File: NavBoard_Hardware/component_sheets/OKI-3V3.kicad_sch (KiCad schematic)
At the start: 4 parts, among them U4 OKI-3V3

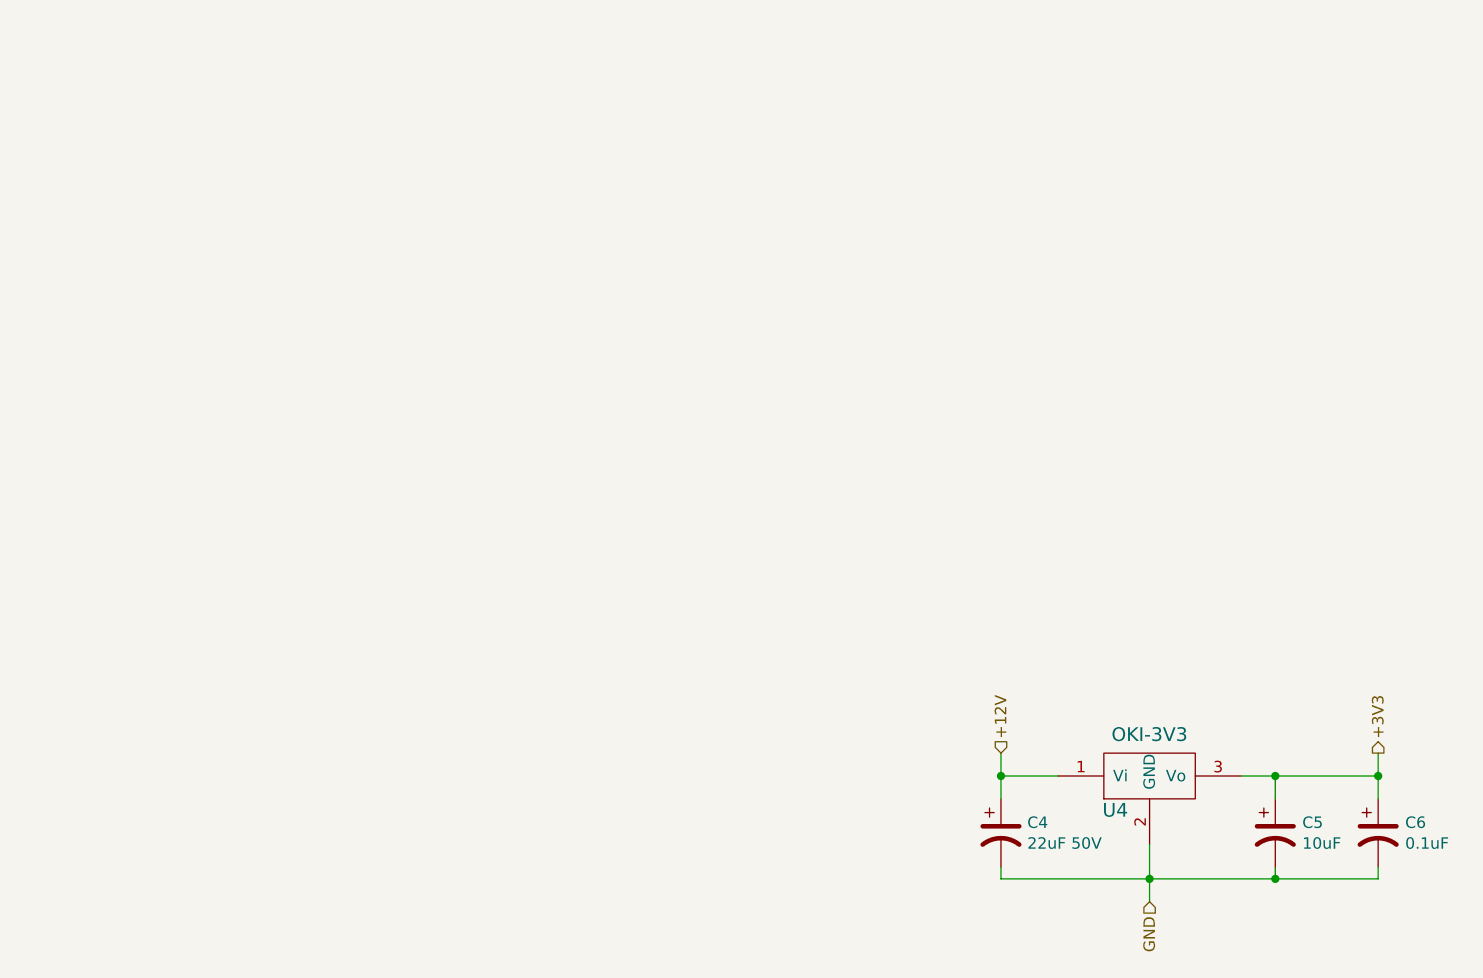
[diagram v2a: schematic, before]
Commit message: Corrected accelerometer regulator capacitors
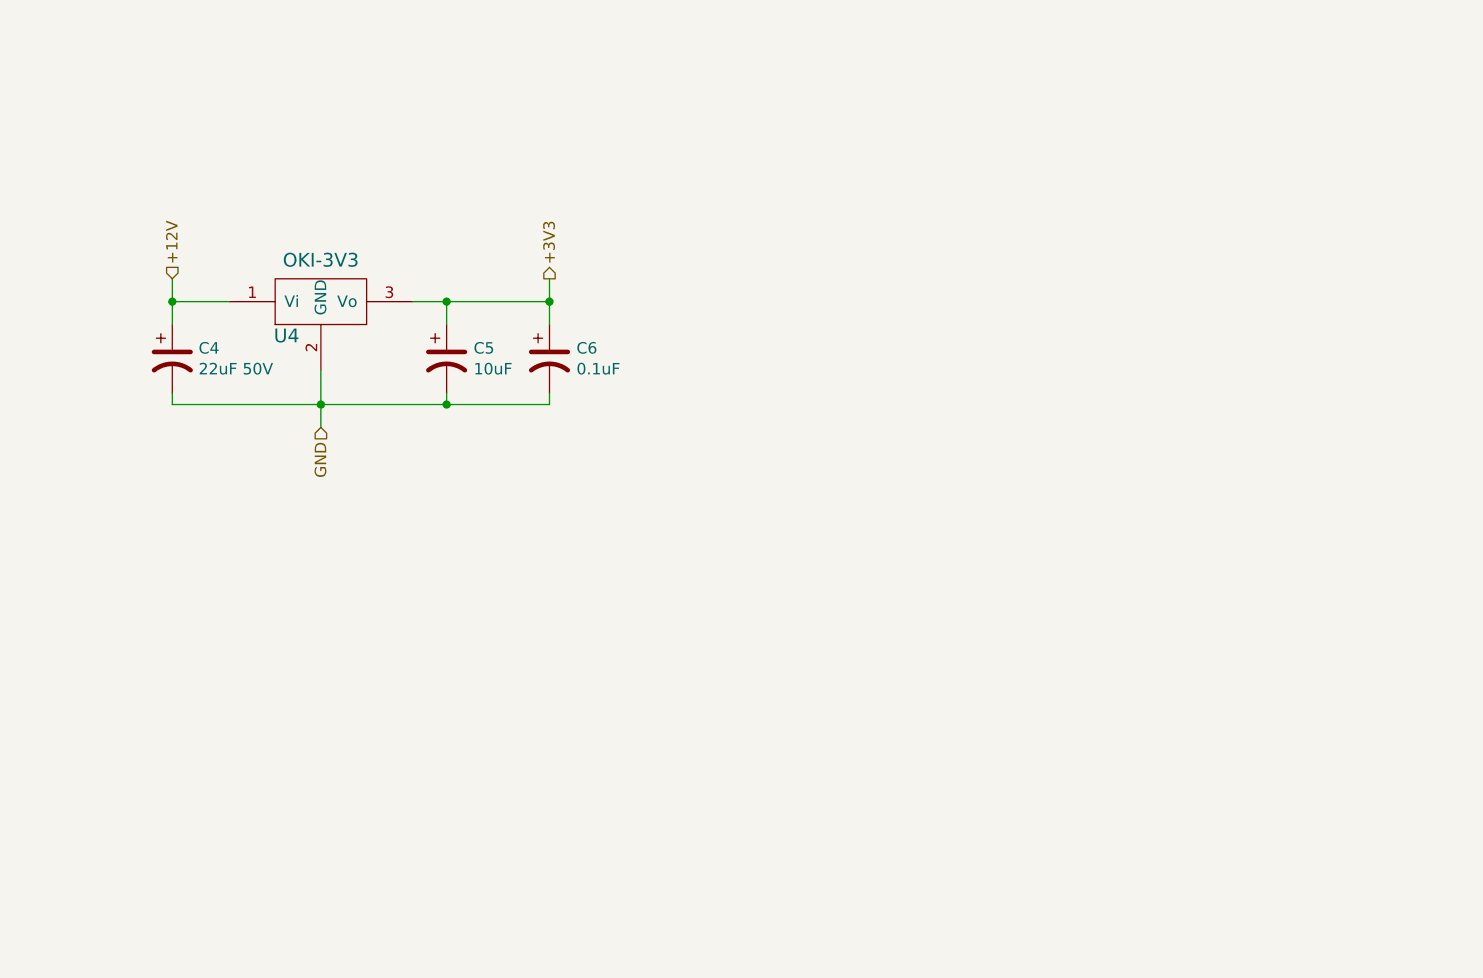
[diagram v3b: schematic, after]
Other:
- moved on the sheet: C4, C5, C6, U4
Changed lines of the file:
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@@
     (comment 2 "Provides Stable 3V3 From 12V")
   )
-  (junction (at 209.55 146.05) (diameter 0) (color 0 0 0 0)
+  (junction (at 117.475 93.345) (diameter 0) (color 0 0 0 0)
   )
-  (junction (at 251.46 146.05) (diameter 0) (color 0 0 0 0)
+  (junction (at 159.385 93.345) (diameter 0) (color 0 0 0 0)
   )
-  (junction (at 240.03 146.05) (diameter 0) (color 0 0 0 0)
+  (junction (at 147.955 93.345) (diameter 0) (color 0 0 0 0)
   )
-  (junction (at 240.03 157.48) (diameter 0) (color 0 0 0 0)
+  (junction (at 147.955 104.775) (diameter 0) (color 0 0 0 0)
   )
-  (junction (at 226.06 157.48) (diameter 0) (color 0 0 0 0)
+  (junction (at 133.985 104.775) (diameter 0) (color 0 0 0 0)
   )
-  (wire (pts (xy 240.03 157.48) (xy 251.46 157.48))
+  (wire (pts (xy 147.955 104.775) (xy 159.385 104.775))
     (stroke (width 0) (type default) (color 0 0 0 0))
   )
-  (wire (pts (xy 226.06 157.48) (xy 240.03 157.48))
+  (wire (pts (xy 133.985 104.775) (xy 147.955 104.775))
     (stroke (width 0) (type default) (color 0 0 0 0))
   )
-  (wire (pts (xy 215.9 146.05) (xy 209.55 146.05))
+  (wire (pts (xy 123.825 93.345) (xy 117.475 93.345))
     (stroke (width 0) (type default) (color 0 0 0 0))
   )
-  (wire (pts (xy 240.03 157.48) (xy 240.03 156.21))
+  (wire (pts (xy 147.955 104.775) (xy 147.955 103.505))
     (stroke (width 0) (type default) (color 0 0 0 0))
   )
-  (wire (pts (xy 240.03 146.05) (xy 251.46 146.05))
+  (wire (pts (xy 147.955 93.345) (xy 159.385 93.345))
     (stroke (width 0) (type default) (color 0 0 0 0))
   )
-  (wire (pts (xy 226.06 153.67) (xy 226.06 157.48))
+  (wire (pts (xy 133.985 100.965) (xy 133.985 104.775))
     (stroke (width 0) (type default) (color 0 0 0 0))
   )
-  (wire (pts (xy 251.46 148.59) (xy 251.46 146.05))
+  (wire (pts (xy 159.385 95.885) (xy 159.385 93.345))
     (stroke (width 0) (type default) (color 0 0 0 0))
   )
-  (wire (pts (xy 251.46 146.05) (xy 251.46 143.51))
+  (wire (pts (xy 159.385 93.345) (xy 159.385 90.805))
     (stroke (width 0) (type default) (color 0 0 0 0))
   )
-  (wire (pts (xy 209.55 143.51) (xy 209.55 146.05))
+  (wire (pts (xy 117.475 90.805) (xy 117.475 93.345))
     (stroke (width 0) (type default) (color 0 0 0 0))
   )
-  (wire (pts (xy 236.22 146.05) (xy 240.03 146.05))
+  (wire (pts (xy 144.145 93.345) (xy 147.955 93.345))
     (stroke (width 0) (type default) (color 0 0 0 0))
   )
-  (wire (pts (xy 209.55 146.05) (xy 209.55 148.59))
+  (wire (pts (xy 117.475 93.345) (xy 117.475 95.885))
     (stroke (width 0) (type default) (color 0 0 0 0))
   )
-  (wire (pts (xy 209.55 157.48) (xy 226.06 157.48))
+  (wire (pts (xy 117.475 104.775) (xy 133.985 104.775))
     (stroke (width 0) (type default) (color 0 0 0 0))
   )
-  (wire (pts (xy 226.06 157.48) (xy 226.06 160.02))
+  (wire (pts (xy 133.985 104.775) (xy 133.985 107.315))
     (stroke (width 0) (type default) (color 0 0 0 0))
   )
-  (wire (pts (xy 240.03 148.59) (xy 240.03 146.05))
+  (wire (pts (xy 147.955 95.885) (xy 147.955 93.345))
     (stroke (width 0) (type default) (color 0 0 0 0))
   )
-  (wire (pts (xy 251.46 157.48) (xy 251.46 156.21))
+  (wire (pts (xy 159.385 104.775) (xy 159.385 103.505))
     (stroke (width 0) (type default) (color 0 0 0 0))
   )
-  (wire (pts (xy 209.55 156.21) (xy 209.55 157.48))
+  (wire (pts (xy 117.475 103.505) (xy 117.475 104.775))
     (stroke (width 0) (type default) (color 0 0 0 0))
   )
-  (hierarchical_label "GND" (shape input) (at 226.06 160.02 270)
+  (hierarchical_label "GND" (shape input) (at 133.985 107.315 270)
     (effects (font (size 1.27 1.27)) (justify right))
   )
-  (hierarchical_label "+3V3" (shape output) (at 251.46 143.51 90)
+  (hierarchical_label "+3V3" (shape output) (at 159.385 90.805 90)
     (effects (font (size 1.27 1.27)) (justify left))
   )
-  (hierarchical_label "+12V" (shape input) (at 209.55 143.51 90)
+  (hierarchical_label "+12V" (shape input) (at 117.475 90.805 90)
     (effects (font (size 1.27 1.27)) (justify left))
   )
-  (symbol (lib_id "MRDT_Devices:OKI") (at 220.98 148.59 0) (unit 1)
+  (symbol (lib_id "MRDT_Devices:OKI") (at 128.905 95.885 0) (unit 1)
     (in_bom yes) (on_board yes)
-    (property "Reference" "U4" (id 0) (at 222.25 149.86 0)
+    (property "Reference" "U4" (id 0) (at 130.175 97.155 0)
       (effects (font (size 1.524 1.524)))
     )
-    (property "Value" "OKI-3V3" (id 1) (at 226.06 141.4526 0)
+    (property "Value" "OKI-3V3" (id 1) (at 133.985 88.7476 0)
       (effects (font (size 1.524 1.524)))
     )
-    (property "Footprint" "MRDT_Devices:OKI_Horizontal" (id 2) (at 215.9 151.13 0)
+    (property "Footprint" "MRDT_Devices:OKI_Horizontal" (id 2) (at 123.825 98.425 0)
       (effects (font (size 1.524 1.524)) hide)
     )
-    (property "Datasheet" "" (id 3) (at 215.9 151.13 0)
+    (property "Datasheet" "" (id 3) (at 123.825 98.425 0)
       (effects (font (size 1.524 1.524)) hide)
     )
@@
     (pin "3")
   )
-  (symbol (lib_id "Device:C_Polarized_US") (at 209.55 152.4 0) (unit 1)
+  (symbol (lib_id "Device:C_Polarized_US") (at 117.475 99.695 0) (unit 1)
     (in_bom yes) (on_board yes)
-    (property "Reference" "C4" (id 0) (at 212.471 151.2316 0)
+    (property "Reference" "C4" (id 0) (at 120.396 98.5266 0)
       (effects (font (size 1.27 1.27)) (justify left))
     )
-    (property "Value" "22uF 50V" (id 1) (at 212.471 153.543 0)
+    (property "Value" "22uF 50V" (id 1) (at 120.396 100.838 0)
       (effects (font (size 1.27 1.27)) (justify left))
     )
-    (property "Footprint" "Capacitor_THT:CP_Radial_D6.3mm_P2.50mm" (id 2) (at 209.55 152.4 0)
+    (property "Footprint" "Capacitor_THT:CP_Radial_D6.3mm_P2.50mm" (id 2) (at 117.475 99.695 0)
       (effects (font (size 1.27 1.27)) hide)
     )
-    (property "Datasheet" "~" (id 3) (at 209.55 152.4 0)
+    (property "Datasheet" "~" (id 3) (at 117.475 99.695 0)
       (effects (font (size 1.27 1.27)) hide)
     )
@@
     (pin "2")
   )
-  (symbol (lib_id "Device:C_Polarized_US") (at 251.46 152.4 0) (unit 1)
+  (symbol (lib_id "Device:C_Polarized_US") (at 159.385 99.695 0) (unit 1)
     (in_bom yes) (on_board yes)
-    (property "Reference" "C6" (id 0) (at 254.4572 151.2316 0)
+    (property "Reference" "C6" (id 0) (at 162.3822 98.5266 0)
       (effects (font (size 1.27 1.27)) (justify left))
     )
-    (property "Value" "0.1uF" (id 1) (at 254.4572 153.543 0)
+    (property "Value" "0.1uF" (id 1) (at 162.3822 100.838 0)
       (effects (font (size 1.27 1.27)) (justify left))
     )
-    (property "Footprint" "Capacitor_SMD:C_0603_1608Metric_Pad1.08x0.95mm_HandSolder" (id 2) (at 251.46 152.4 0)
+    (property "Footprint" "Capacitor_SMD:C_0603_1608Metric_Pad1.08x0.95mm_HandSolder" (id 2) (at 159.385 99.695 0)
       (effects (font (size 1.27 1.27)) hide)
     )
-    (property "Datasheet" "~" (id 3) (at 251.46 152.4 0)
+    (property "Datasheet" "~" (id 3) (at 159.385 99.695 0)
       (effects (font (size 1.27 1.27)) hide)
     )
@@
     (pin "2")
   )
-  (symbol (lib_id "Device:C_Polarized_US") (at 240.03 152.4 0) (unit 1)
+  (symbol (lib_id "Device:C_Polarized_US") (at 147.955 99.695 0) (unit 1)
     (in_bom yes) (on_board yes)
-    (property "Reference" "C5" (id 0) (at 243.0272 151.2316 0)
+    (property "Reference" "C5" (id 0) (at 150.9522 98.5266 0)
       (effects (font (size 1.27 1.27)) (justify left))
     )
-    (property "Value" "10uF" (id 1) (at 243.0272 153.543 0)
+    (property "Value" "10uF" (id 1) (at 150.9522 100.838 0)
       (effects (font (size 1.27 1.27)) (justify left))
     )
-    (property "Footprint" "Capacitor_SMD:C_0603_1608Metric_Pad1.08x0.95mm_HandSolder" (id 2) (at 240.03 152.4 0)
+    (property "Footprint" "Capacitor_SMD:C_0603_1608Metric_Pad1.08x0.95mm_HandSolder" (id 2) (at 147.955 99.695 0)
       (effects (font (size 1.27 1.27)) hide)
     )
-    (property "Datasheet" "~" (id 3) (at 240.03 152.4 0)
+    (property "Datasheet" "~" (id 3) (at 147.955 99.695 0)
       (effects (font (size 1.27 1.27)) hide)
     )
